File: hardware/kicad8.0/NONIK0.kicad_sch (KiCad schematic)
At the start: 16 parts, among them J1 AVR-UPDI-6, J2 Qwiic/Stemma QT, J3 Test Pads, SW1 SW_SPST, SW2 SW_Push, SW3 SW_Push, U1 HCMS-291X, U2 ATtiny1604-SS

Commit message: buzzer
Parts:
- added BZ1: Buzzer, NONIK0:CMT-322-65-SMT-TR, symbol Device:Buzzer
- added R2: 1K, NONIK0:R_0603_1608Metric, symbol Device:R
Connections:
- net GND: now also U1.25 (OSC), BZ1.2 (-)
- net OSC renamed BUZZ
- net BUZZ: now also R2.2; no longer U1.25 (OSC)
- new net: BZ1.1 (+), R2.1

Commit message: adding power reg and piezo
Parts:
- added C1, C3: 10u, NONIK0:C_0603_1608Metric, symbol PCM_SL_Devices:Capacitor_NP
- added C2: 1u, NONIK0:C_0603_1608Metric, symbol PCM_SL_Devices:Capacitor_NP
- added JP1: SolderJumper_2_Bridged, Jumper:SolderJumper-3_P1.3mm_Bridged2Bar12_RoundedPad1.0x1.5mm, symbol Jumper:SolderJumper_2_Bridged
- added U3: AP3602A, NONIK0:SOT-23-6, symbol NONIK0:AP3602A
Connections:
- net GND: now also C1.1, C3.1, U3.2 (GND)
- net VCC: now also C1.2, JP1.2 (B), U3.3 (~{SHDN}), U3.5 (VIN); no longer U1.10 (V_LED), U1.3 (V_LED)
- new net: C2.1, U3.6 (C+)
- new net: C2.2, U3.4 (C-)
- new net Vled: C3.2, JP1.1 (A), U1.10 (V_LED), U1.3 (V_LED), U3.1 (VOUT)
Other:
- note added: "Buzzer"
- note added: "Cut JP1 if populating U3"
- note added: "Optional"
- moved on the sheet: BT1, BT2, BZ1, D1, H1, H2, H3, H4, J3, R1, R2, SW1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

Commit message: pcb done, pending review
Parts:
- JP1: footprint Jumper:SolderJumper-3_P1.3mm_Bridged2Bar12_RoundedPad1.0x1.5mm -> NONIK0:SolderJumper-2_P1.3mm_Bridged_RoundedPad1.0x1.5mm
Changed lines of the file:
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@@
 			)
 		)
-		(property "Footprint" "Jumper:SolderJumper-3_P1.3mm_Bridged2Bar12_RoundedPad1.0x1.5mm"
+		(property "Footprint" "NONIK0:SolderJumper-2_P1.3mm_Bridged_RoundedPad1.0x1.5mm"
 			(at 62.23 132.08 0)
 			(effects

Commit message: fit and finish things
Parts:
- J1: value AVR-UPDI-6 -> AVR-UPDI-3
- U1: value HCMS-291X -> LED_HCMS-2915
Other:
- moved on the sheet: U1

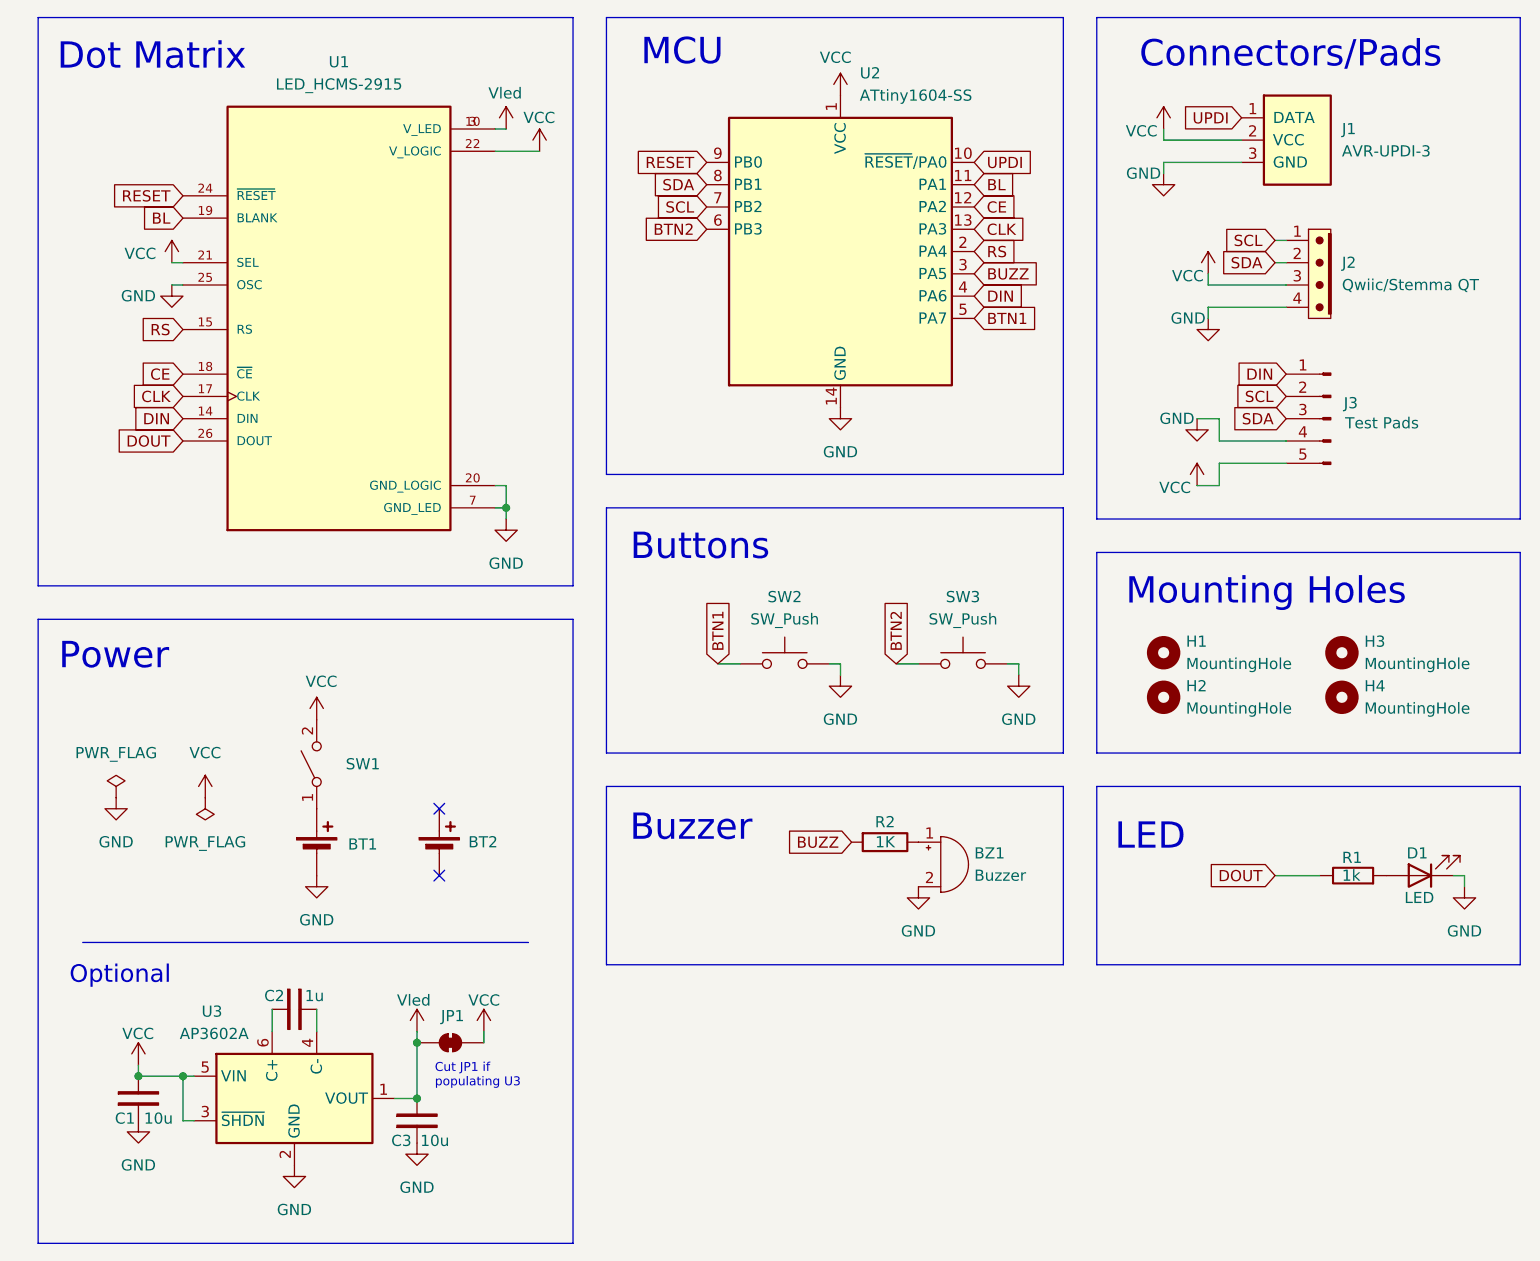
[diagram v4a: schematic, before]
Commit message: more test pads
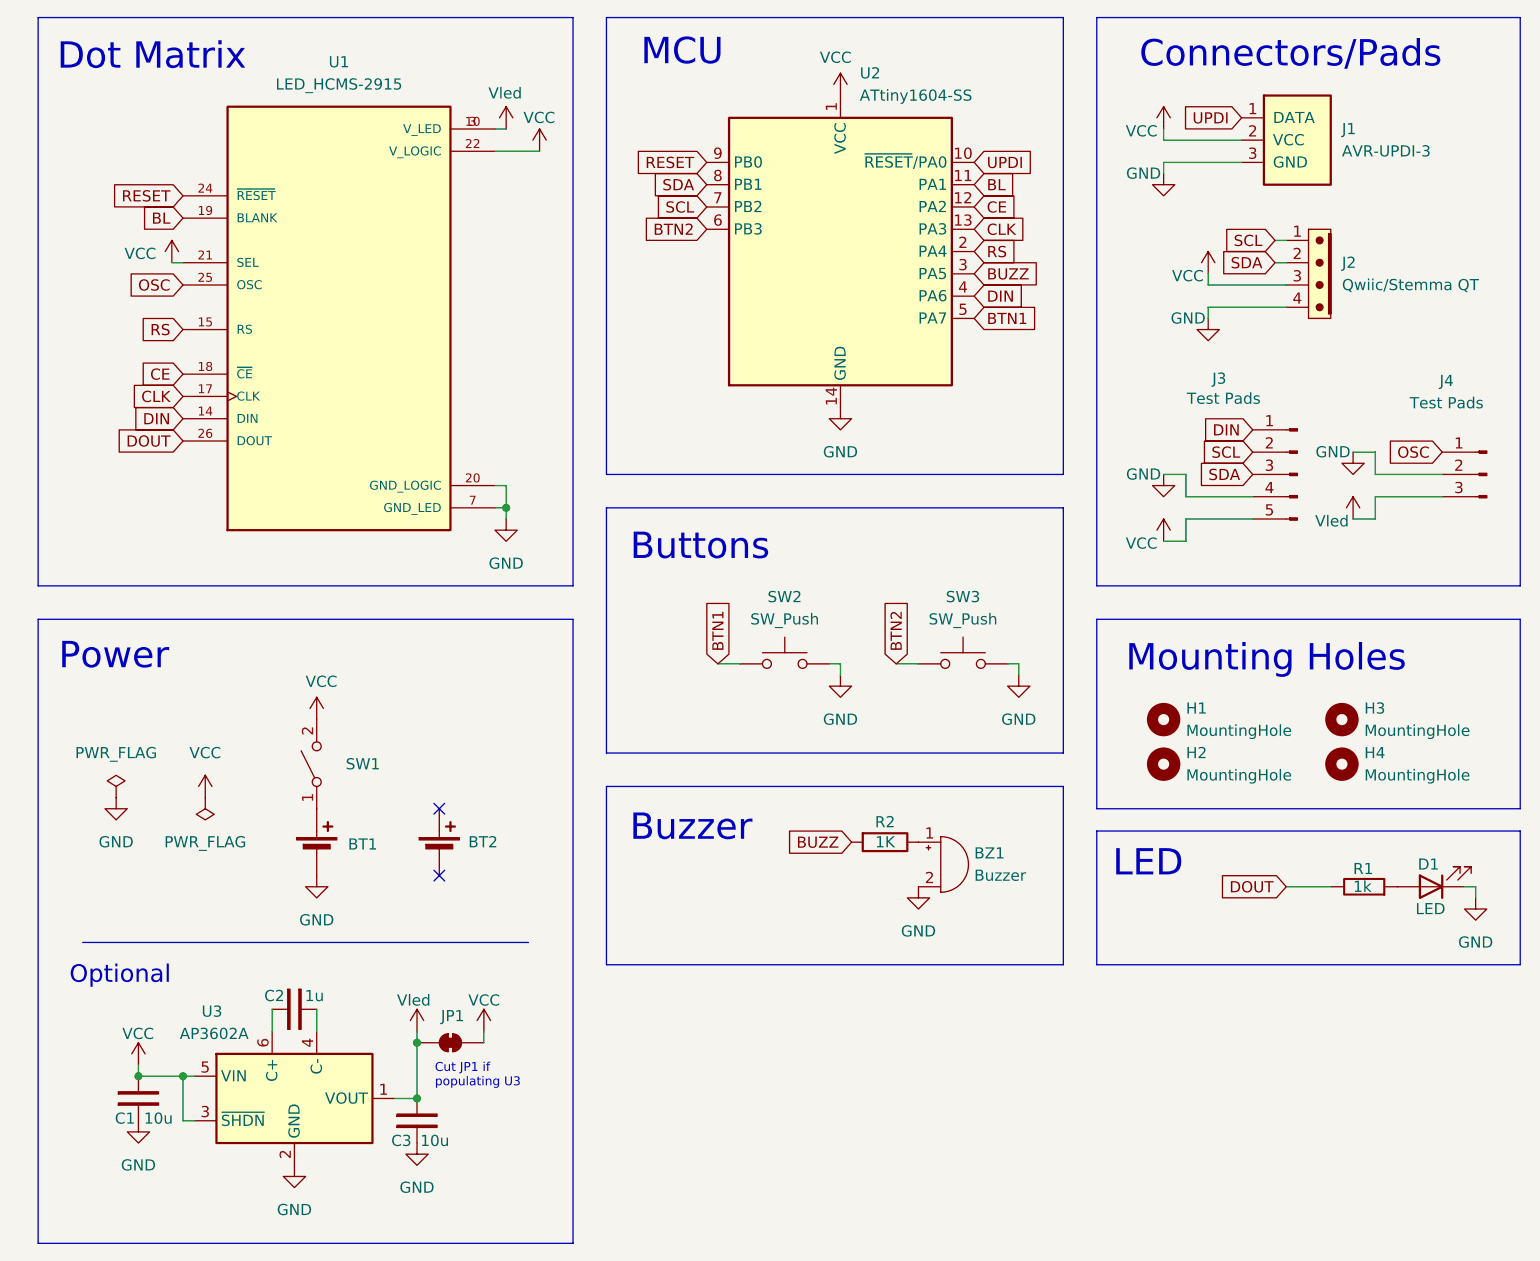
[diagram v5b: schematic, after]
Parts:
- added J4: Test Pads, NONIK0:Pads_1x3_2.54mm, symbol Connector:Conn_01x03_Pin
- J1: footprint NONIK0:UPDI_Pads -> NONIK0:Pads_1x3_2.54mm
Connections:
- net GND: now also J4.2 (Pin_2); no longer U1.25 (OSC)
- net Vled: now also J4.3 (Pin_3)
- new net OSC: J4.1 (Pin_1), U1.25 (OSC)
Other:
- moved on the sheet: D1, H1, H2, H3, H4, J3, R1

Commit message: pcb revisions
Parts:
- added JP2: SolderJumper_3_Bridged12, Jumper:SolderJumper-3_P1.3mm_Bridged12_RoundedPad1.0x1.5mm, symbol Jumper:SolderJumper_3_Bridged12
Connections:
- net GND: now also J4.3 (Pin_3), JP2.3 (B); no longer J4.2 (Pin_2)
- net VCC: now also JP2.1 (A); no longer U1.21 (SEL)
- net Vled: now also J4.2 (Pin_2); no longer J4.3 (Pin_3)
- new net: JP2.2 (C), U1.21 (SEL)

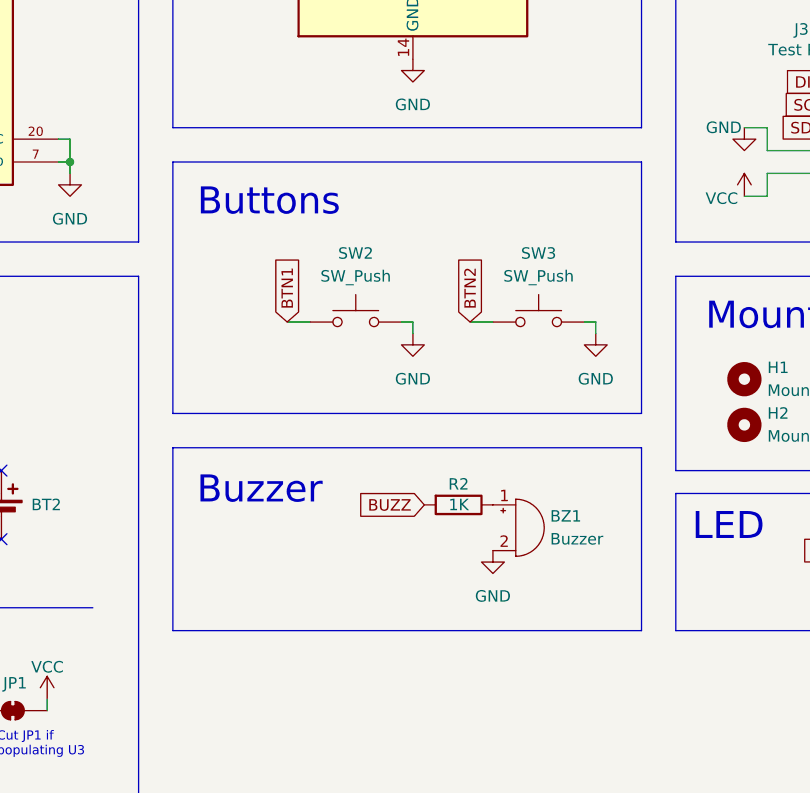
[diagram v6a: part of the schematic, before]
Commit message: adding bjt to drive buzzer
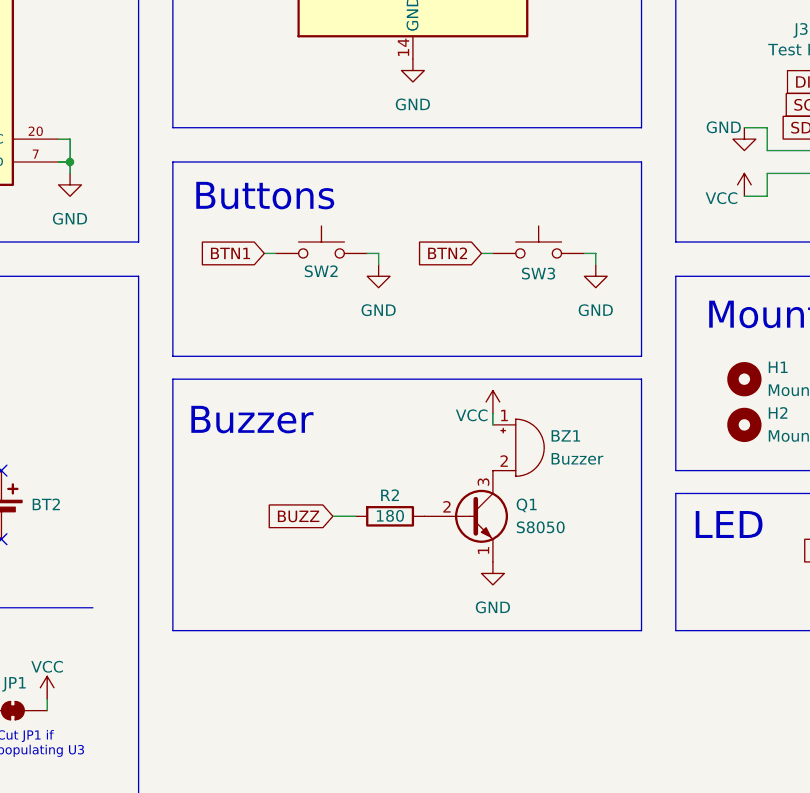
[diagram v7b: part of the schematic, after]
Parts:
- added Q1: S8050, NONIK0:SOT-23-SmallerCourtyard, symbol Transistor_BJT:S8050
- JP2: footprint Jumper:SolderJumper-3_P1.3mm_Bridged12_RoundedPad1.0x1.5mm -> NONIK0:SolderJumper-3_P1.3mm_Bridged12_RoundedPad1.0x1.5mm
- R2: value 1K -> 180
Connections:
- net GND: now also Q1.1 (E); no longer BZ1.2 (-)
- net VCC: now also BZ1.1 (+)
- net at R2.1: now also Q1.2 (B); no longer BZ1.1 (+)
- new net: BZ1.2 (-), Q1.3 (C)
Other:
- moved on the sheet: R2, SW2, SW3

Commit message: pcb fixes, in progress
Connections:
- net RESET: now also U2.7 (PB2); no longer U2.9 (PB0)
- net SCL: now also U2.9 (PB0); no longer U2.7 (PB2)
